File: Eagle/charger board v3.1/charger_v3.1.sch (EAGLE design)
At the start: 32 parts, among them IC1 IR2110D, Q1 2N7000, Q2 IRFP240, Q3 MJE13003G

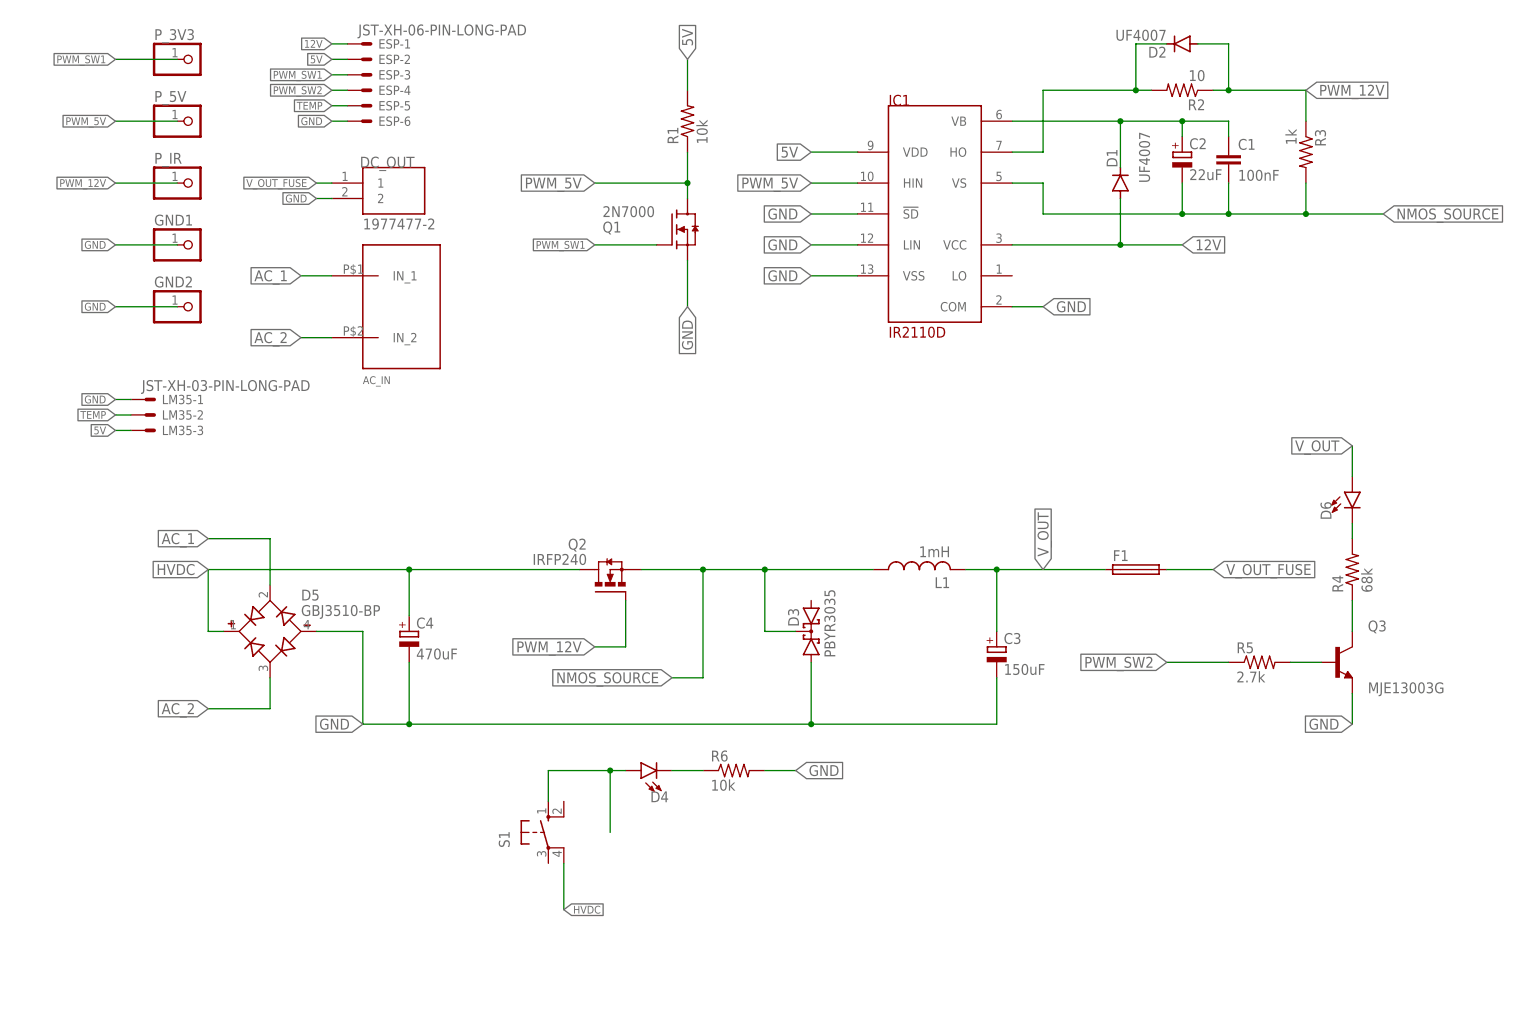
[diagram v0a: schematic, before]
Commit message: buat board charger v3.1
spdt relay
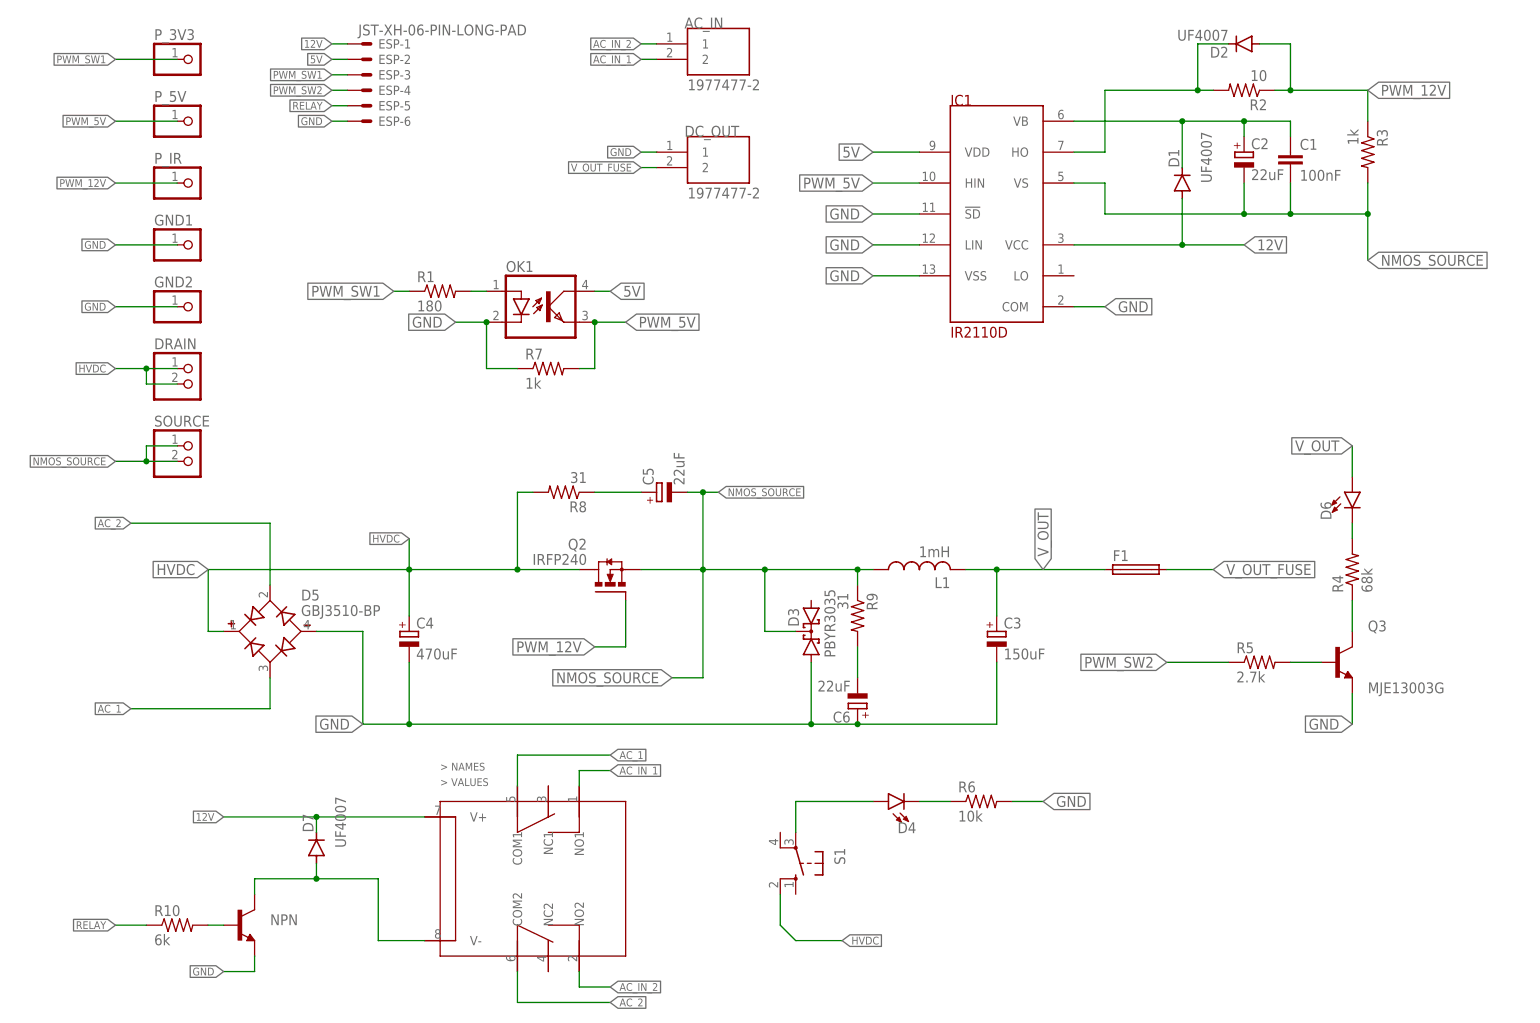
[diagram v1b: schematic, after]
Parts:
- removed LM35: JST-XH-03-PIN-LONG-PAD, Rembrandt Electronics - JST XH Connectors v1-0:JST-XH-03-PIN-LONG-PAD
- removed Q1: 2N7000, 2N7000:2N7000
- added C5, C6: 22uF, rcl:CPOL-EUE7.5-18
- added D7: UF4007, diode:BAS15
- added DRAIN, SOURCE: (no value), pinhead:PINHD-1X2
- added NPN: (no value), transistor:BC547A-NPN-TO92-CBE
- added OK1: SFH618A-5, optocoupler:SFH618A-5
- added R10: 6k, rcl:R-US_0204/7
- added R7: 1k, rcl:R-US_0204/7
- added R8, R9: 31, rcl:R-US_0411/15
- added U$1: DPDT-HK19F, TA_library:DPDT-HK19F
- AC_IN: value XT90A -> 1977477-2; device TA_library:XT90A -> terminal_block_TA:1977477-2
- F1: device fuse:SH25 -> TA_library:FUSEHOLDER
- R1: value 10k -> 180
- R4: device rcl:R-US_0309/12 -> rcl:R-US_0411/15
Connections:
- removed net TEMP: ESP-5.S, LM35-2.S
- new net AC_IN_1: AC_IN.2, U$1.NO1
- new net AC_IN_2: AC_IN.1, U$1.NO2
- new net N$13: NPN.B, R10.2
- new net N$14: D7.A, NPN.C, U$1.V-
- new net N$6: C5.+, R8.1
- new net N$7: C6.-, R9.2
- new net N$9: OK1.A, R1.2
- new net RELAY: ESP-5.S, R10.1
- net 12V: now also D7.C, U$1.V+
- net 5V: now also OK1.COL; no longer LM35-3.S, R1.2
- net AC_1: now also D5.AC2, U$1.COM1; no longer AC_IN.IN_1, D5.AC1
- net AC_2: now also D5.AC1, U$1.COM2; no longer AC_IN.IN_2, D5.AC2
- net GND: now also C6.+, DC_OUT.1, NPN.E, OK1.C, R7.1; no longer DC_OUT.2, LM35-1.S, Q1.S
- net HVDC: now also DRAIN.1, DRAIN.2, R8.2, S1.S1; no longer S1.P1
- net N$2: now also S1.P; no longer S1.S
- net NMOS_SOURCE: now also C5.-, R9.1, SOURCE.1, SOURCE.2
- net PWM_5V: now also OK1.EMIT, R7.2; no longer Q1.D, R1.1
- net PWM_SW1: now also R1.1; no longer Q1.G
- net V_OUT_FUSE: now also DC_OUT.2; no longer DC_OUT.1
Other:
- moved on the sheet: AC_IN, C1, C2, C3, D1, D2, D4, DC_OUT, IC1, R1, R2, R3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
